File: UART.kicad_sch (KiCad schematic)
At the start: 27 parts, among them J22 430450212, J23 430450612, J24 430450212, U5 MAX485, U7 ISOW1432BDFMR

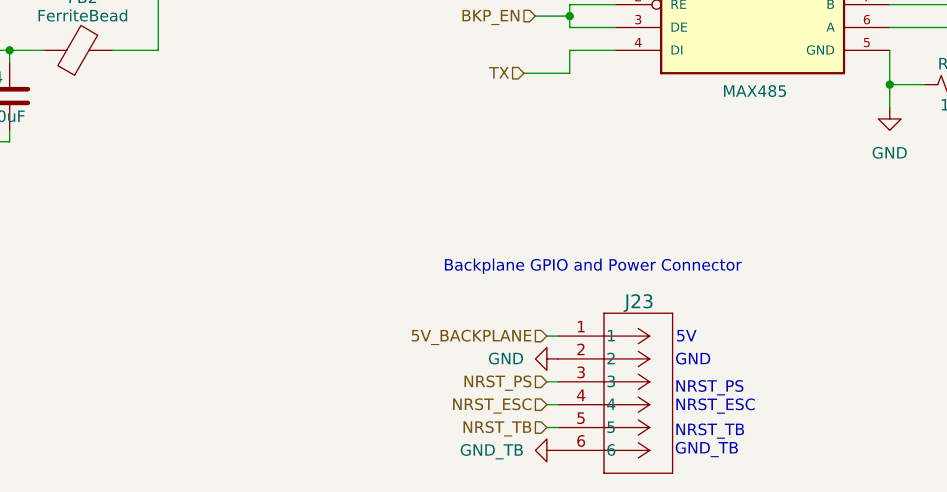
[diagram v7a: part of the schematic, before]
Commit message: Added header and updated mounting pins
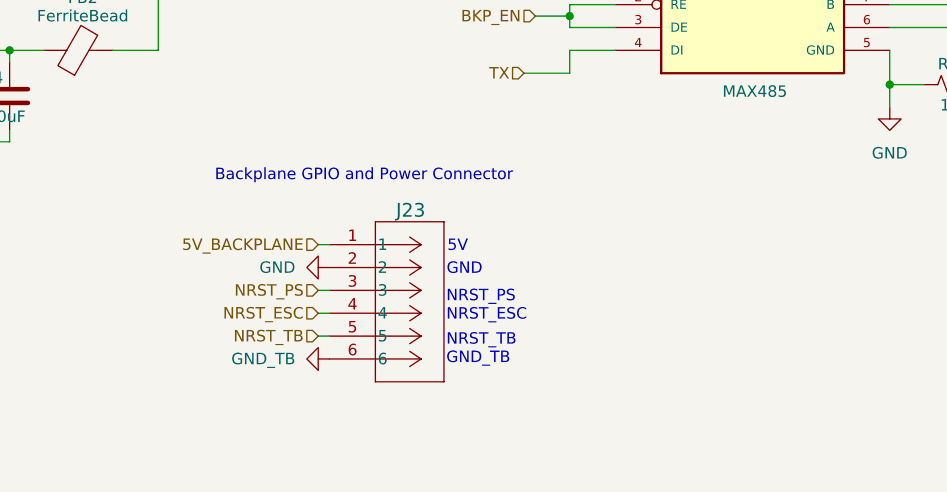
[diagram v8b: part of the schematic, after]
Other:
- moved on the sheet: J23
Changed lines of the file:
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@@
 	(wire
 		(pts
-			(xy 199.39 152.4) (xy 200.66 152.4)
+			(xy 173.99 142.24) (xy 175.26 142.24)
 		)
 		(stroke
@@
 	(wire
 		(pts
-			(xy 199.39 154.94) (xy 200.66 154.94)
+			(xy 173.99 144.78) (xy 175.26 144.78)
 		)
 		(stroke
@@
 	(wire
 		(pts
-			(xy 199.39 144.78) (xy 200.66 144.78)
+			(xy 173.99 134.62) (xy 175.26 134.62)
 		)
 		(stroke
@@
 	(wire
 		(pts
-			(xy 200.66 149.86) (xy 199.39 149.86)
+			(xy 175.26 139.7) (xy 173.99 139.7)
 		)
 		(stroke
@@
 	(text "GND"
 		(exclude_from_sim no)
-		(at 215.646 147.574 0)
+		(at 190.246 137.414 0)
 		(effects
 			(font
@@
 	(text "NRST_TB\nGND_TB"
 		(exclude_from_sim no)
-		(at 213.614 156.464 0)
+		(at 188.214 146.304 0)
 		(effects
 			(font
@@
 	(text "NRST_PS\nNRST_ESC"
 		(exclude_from_sim no)
-		(at 213.614 151.638 0)
+		(at 188.214 141.478 0)
 		(effects
 			(font
@@
 	(text "Backplane GPIO and Power Connector"
 		(exclude_from_sim no)
-		(at 204.47 137.16 0)
+		(at 179.07 127 0)
 		(effects
 			(font
@@
 	(text "5V\n\n"
 		(exclude_from_sim no)
-		(at 214.884 146.05 0)
+		(at 189.484 135.89 0)
 		(effects
 			(font
@@
 	(hierarchical_label "NRST_ESC"
 		(shape input)
-		(at 199.39 152.4 180)
+		(at 173.99 142.24 180)
 		(fields_autoplaced yes)
 		(effects
@@
 	(hierarchical_label "5V_BACKPLANE"
 		(shape input)
-		(at 199.39 144.78 180)
+		(at 173.99 134.62 180)
 		(fields_autoplaced yes)
 		(effects
@@
 	(hierarchical_label "NRST_TB"
 		(shape input)
-		(at 199.39 154.94 180)
+		(at 173.99 144.78 180)
 		(fields_autoplaced yes)
 		(effects
@@
 	(hierarchical_label "NRST_PS"
 		(shape input)
-		(at 199.39 149.86 180)
+		(at 173.99 139.7 180)
 		(fields_autoplaced yes)
 		(effects
@@
 	(symbol
 		(lib_id "power:GND")
-		(at 200.66 147.32 270)
+		(at 175.26 137.16 270)
 		(unit 1)
 		(exclude_from_sim no)
@@
 		(fields_autoplaced yes)
 		(property "Reference" "#PWR021"
-			(at 194.31 147.32 0)
+			(at 168.91 137.16 0)
 			(effects
 				(font
@@
 		)
 		(property "Value" "GND"
-			(at 196.85 147.3199 90)
+			(at 171.45 137.1599 90)
 			(effects
 				(font
@@
 		)
 		(property "Footprint" ""
-			(at 200.66 147.32 0)
+			(at 175.26 137.16 0)
 			(effects
 				(font
@@
 		)
 		(property "Datasheet" ""
-			(at 200.66 147.32 0)
+			(at 175.26 137.16 0)
 			(effects
 				(font
@@
 		)
 		(property "Description" "Power symbol creates a global label with name \"GND\" , ground"
-			(at 200.66 147.32 0)
+			(at 175.26 137.16 0)
 			(effects
 				(font
@@
 	(symbol
 		(lib_id "CON_430450612_MOL:430450612")
-		(at 200.66 144.78 0)
+		(at 175.26 134.62 0)
 		(unit 1)
 		(exclude_from_sim no)
@@
 		(dnp no)
 		(property "Reference" "J23"
-			(at 208.026 140.97 0)
+			(at 182.626 130.81 0)
 			(effects
 				(font
@@
 		)
 		(property "Value" "430450612"
-			(at 214.63 152.3999 0)
+			(at 189.23 142.2399 0)
 			(effects
 				(font
@@
 		)
 		(property "Footprint" "CON_430450612_MOL:CON_430450612_MOL"
-			(at 200.66 144.78 0)
+			(at 175.26 134.62 0)
 			(effects
 				(font
@@
 		)
 		(property "Datasheet" "430450612"
-			(at 200.66 144.78 0)
+			(at 175.26 134.62 0)
 			(effects
 				(font
@@
 		)
 		(property "Description" ""
-			(at 200.66 144.78 0)
+			(at 175.26 134.62 0)
 			(effects
 				(font
@@
 	(symbol
 		(lib_id "power:GND")
-		(at 200.66 157.48 270)
+		(at 175.26 147.32 270)
 		(unit 1)
 		(exclude_from_sim no)
@@
 		(fields_autoplaced yes)
 		(property "Reference" "#PWR068"
-			(at 194.31 157.48 0)
+			(at 168.91 147.32 0)
 			(effects
 				(font
@@
 		)
 		(property "Value" "GND_TB"
-			(at 196.85 157.4799 90)
+			(at 171.45 147.3199 90)
 			(effects
 				(font
@@
 		)
 		(property "Footprint" ""
-			(at 200.66 157.48 0)
+			(at 175.26 147.32 0)
 			(effects
 				(font
@@
 		)
 		(property "Datasheet" ""
-			(at 200.66 157.48 0)
+			(at 175.26 147.32 0)
 			(effects
 				(font
@@
 		)
 		(property "Description" "Power symbol creates a global label with name \"GND\" , ground"
-			(at 200.66 157.48 0)
+			(at 175.26 147.32 0)
 			(effects
 				(font
